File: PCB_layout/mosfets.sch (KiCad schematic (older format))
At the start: 45 parts, among them CN10 OUT, CN11 OUT, CN12 OUT, CN13 OUT, CN9 OUT, Q3 IRLR7843TRPBF, Q4 IRLR7843TRPBF, Q5 IRLR7843TRPBF, Q6 IRLR7843TRPBF, Q7 IRLR7843TRPBF

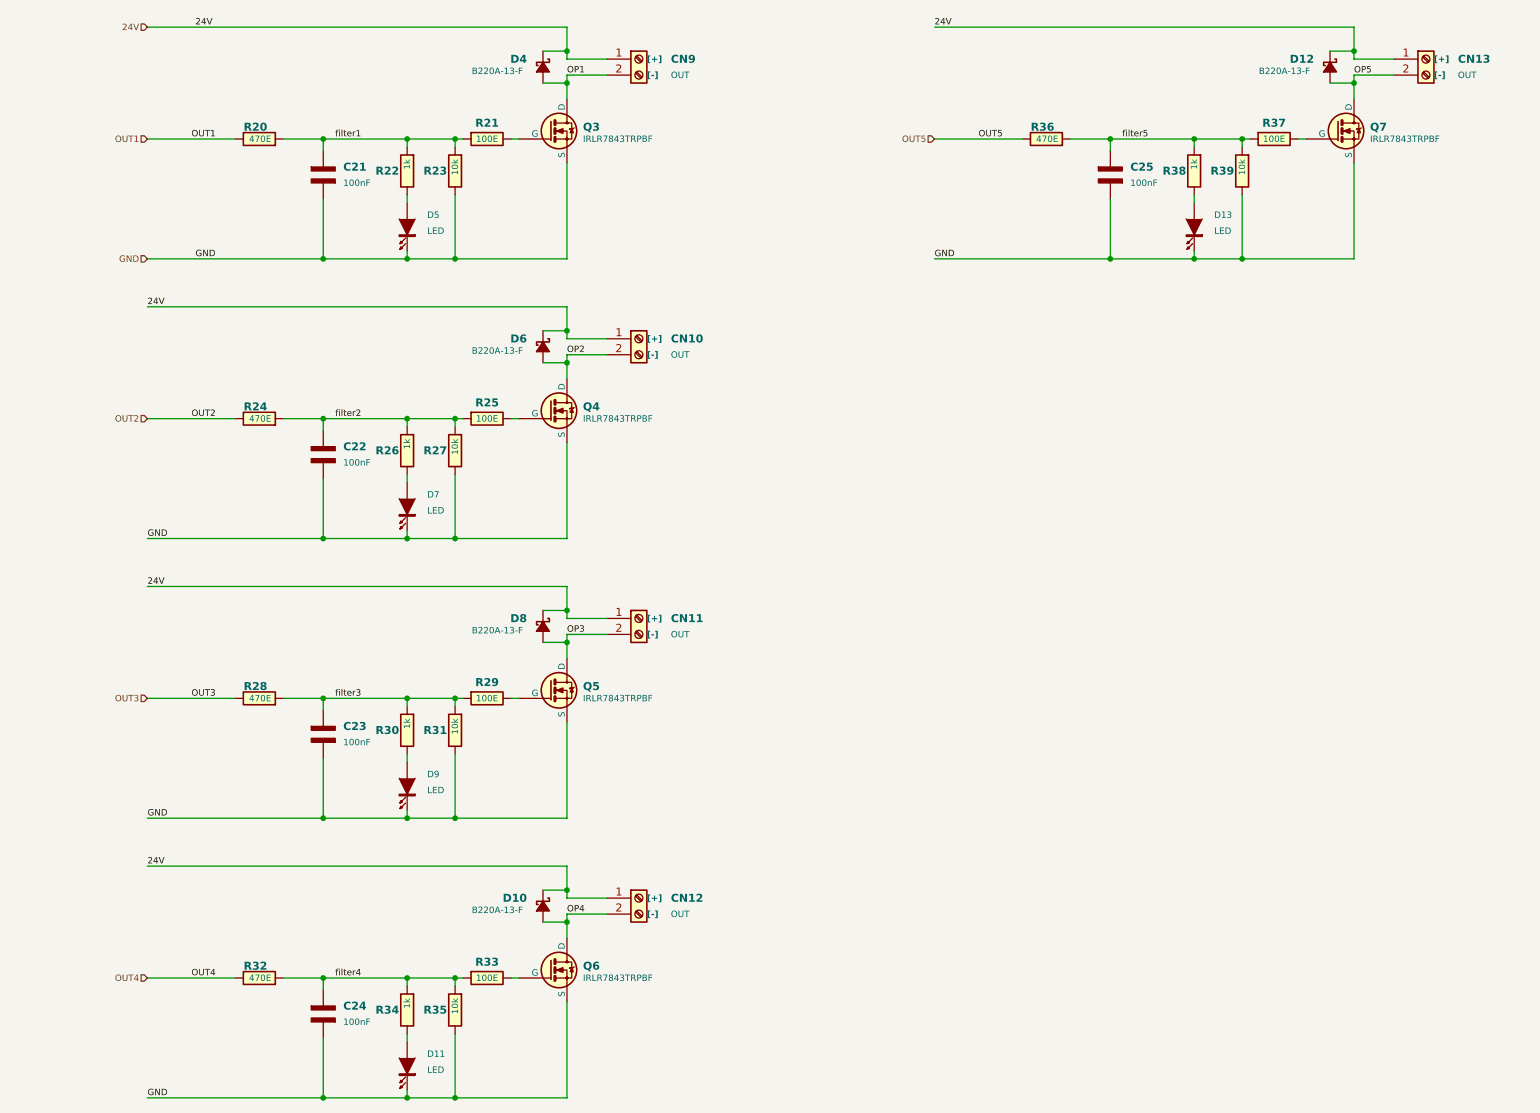
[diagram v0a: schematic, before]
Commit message: added optocoupler for isolation
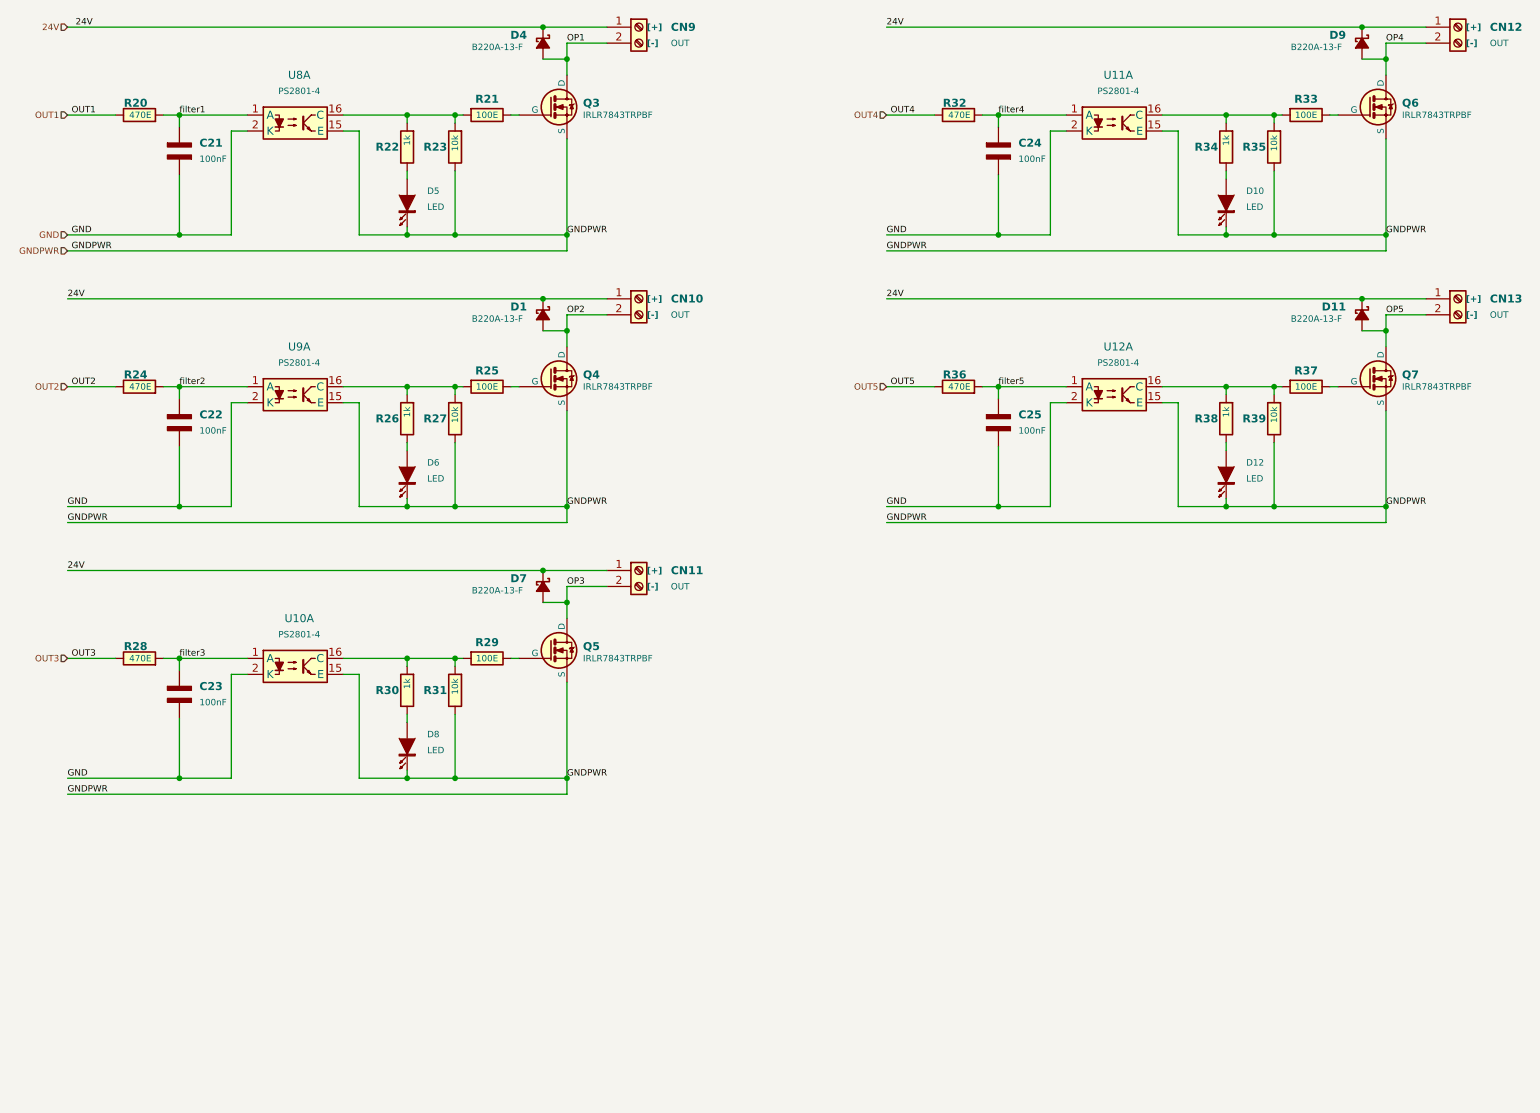
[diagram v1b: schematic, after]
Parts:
- removed D10, D12, D6, D8: B220A-13-F, AA_vayu:D_SMB, symbol AA_vayuO2_symbols:D_Schottky_Small
- removed D11, D13, D7, D9: LED, AA_vayu:LED_0603_1608Metric, symbol AA_vayuO2_symbols:LED
- added D1, D11, D7, D9: B220A-13-F, AA_vayu:D_SMB, symbol AA_vayuO2_symbols:D_Schottky_Small
- added D10, D12, D6, D8: LED, AA_vayu:LED_0603_1608Metric, symbol AA_vayuO2_symbols:LED
- added U10, U11, U12, U8, U9: PS2801-4, symbol AA_vayuO2_symbols:PS2801-4
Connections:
- net 24V: now also D1.1 (K), D11.1 (K), D7.1 (K), D9.1 (K)
- net GND: now also U10.2 (K), U11.2 (K), U12.2 (K), U8.2 (K), U9.2 (K); no longer D5.2 (K), Q3.3 (S), Q4.3 (S), Q5.3 (S), Q6.3 (S), Q7.3 (S), R23.1, R27.1, R31.1, R35.1, R39.1
- net OP2: now also D1.2 (A)
- net OP3: now also D7.2 (A)
- net OP4: now also D9.2 (A)
- net OP5: now also D11.2 (A)
- net filter1: now also U8.1 (A); no longer R21.2, R22.2, R23.2
- net filter2: now also U9.1 (A); no longer R25.2, R26.2, R27.2
- net filter3: now also U10.1 (A); no longer R29.2, R30.2, R31.2
- net filter4: now also U11.1 (A); no longer R33.2, R34.2, R35.2
- net filter5: now also U12.1 (A); no longer R37.2, R38.2, R39.2
- net at R26.1: now also D6.1 (A)
- net at R30.1: now also D8.1 (A)
- net at R34.1: now also D10.1 (A)
- net at R38.1: now also D12.1 (A)
- new net: R21.2, R22.2, R23.2, U8.16 (C)
- new net: R25.2, R26.2, R27.2, U9.16 (C)
- new net: R29.2, R30.2, R31.2, U10.16 (C)
- new net: R33.2, R34.2, R35.2, U11.16 (C)
- new net: R37.2, R38.2, R39.2, U12.16 (C)
- new net GNDPWR: D10.2 (K), D12.2 (K), D5.2 (K), D6.2 (K), D8.2 (K), Q3.3 (S), Q4.3 (S), Q5.3 (S), Q6.3 (S), Q7.3 (S), R23.1, R27.1, R31.1, R35.1, R39.1, U10.15 (E), U11.15 (E), U12.15 (E), U8.15 (E), U9.15 (E)
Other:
- moved on the sheet: C21, CN9, D4, D5, Q3, R20, R21, R22, R23

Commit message: PCB layout, WIP
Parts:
- U8: footprint (none) -> AA_vayu:SO-16_5.3x10.2mm_P1.27mm
- U8: renamed from U9; footprint (none) -> AA_vayu:SO-16_5.3x10.2mm_P1.27mm
- U8: renamed from U10; footprint (none) -> AA_vayu:SO-16_5.3x10.2mm_P1.27mm
- U8: renamed from U11; footprint (none) -> AA_vayu:SO-16_5.3x10.2mm_P1.27mm
- U9: renamed from U12; footprint (none) -> AA_vayu:SO-4_5.3x2.7mm_P1.27mm
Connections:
- net GND: now also U8.4 (K), U8.6 (K), U8.8 (K); no longer U8.2 (K), U8.2 (K), U8.2 (K)
- net GNDPWR: now also U8.11 (K), U8.13 (E), U8.9 (E); no longer U8.15 (E), U8.15 (E), U8.15 (E)
- net filter2: now also U8.3 (A); no longer U8.1 (A)
- net filter3: now also U8.5 (A); no longer U8.1 (A)
- net filter4: now also U8.7 (A); no longer U8.1 (A)
- net at R25.2, R26.2, R27.2: now also U8.14 (C); no longer U8.16 (C)
- net at R29.2, R30.2, R31.2: now also U8.12 (C); no longer U8.16 (C)
- net at R33.2, R34.2, R35.2: now also U8.10 (C); no longer U8.16 (C)
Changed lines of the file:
@@
 F 0 "U8" H 2350 1725 50  0000 C CNN
 F 1 "PS2801-4" H 2350 1625 40  0000 C CNN
-F 2 "" H 2325 1125 50  0001 C CIN
+F 2 "AA_vayu:SO-16_5.3x10.2mm_P1.27mm" H 2325 1125 50  0001 C CIN
 F 3 "" H 2300 1400 50  0001 L CNN
 	1    2325 1425
@@
 	4025 2725 4025 2625
 $Comp
-L AA_vayuO2_symbols:PS2801-4 U9
-U 1 1 61650FE4
+L AA_vayuO2_symbols:PS2801-4 U8
+U 2 1 61650FE4
 P 2325 3125
-F 0 "U9" H 2350 3425 50  0000 C CNN
+F 0 "U8" H 2350 3425 50  0000 C CNN
 F 1 "PS2801-4" H 2350 3325 40  0000 C CNN
-F 2 "" H 2325 2825 50  0001 C CIN
+F 2 "AA_vayu:SO-16_5.3x10.2mm_P1.27mm" H 2325 2825 50  0001 C CIN
 F 3 "" H 2300 3100 50  0001 L CNN
-	1    2325 3125
+	2    2325 3125
 	1    0    0    -1
 $EndComp
@@
 	4025 4425 4025 4325
 $Comp
-L AA_vayuO2_symbols:PS2801-4 U10
-U 1 1 6165FC0E
+L AA_vayuO2_symbols:PS2801-4 U8
+U 3 1 6165FC0E
 P 2325 4825
-F 0 "U10" H 2350 5125 50  0000 C CNN
+F 0 "U8" H 2350 5125 50  0000 C CNN
 F 1 "PS2801-4" H 2350 5025 40  0000 C CNN
-F 2 "" H 2325 4525 50  0001 C CIN
+F 2 "AA_vayu:SO-16_5.3x10.2mm_P1.27mm" H 2325 4525 50  0001 C CIN
 F 3 "" H 2300 4800 50  0001 L CNN
-	1    2325 4825
+	3    2325 4825
 	1    0    0    -1
 $EndComp
@@
 	9150 1025 9150 925
 $Comp
-L AA_vayuO2_symbols:PS2801-4 U11
-U 1 1 6165FCB0
+L AA_vayuO2_symbols:PS2801-4 U8
+U 4 1 6165FCB0
 P 7450 1425
-F 0 "U11" H 7475 1725 50  0000 C CNN
+F 0 "U8" H 7475 1725 50  0000 C CNN
 F 1 "PS2801-4" H 7475 1625 40  0000 C CNN
-F 2 "" H 7450 1125 50  0001 C CIN
+F 2 "AA_vayu:SO-16_5.3x10.2mm_P1.27mm" H 7450 1125 50  0001 C CIN
 F 3 "" H 7425 1400 50  0001 L CNN
-	1    7450 1425
+	4    7450 1425
 	1    0    0    -1
 $EndComp
@@
 	9150 2725 9150 2625
 $Comp
-L AA_vayuO2_symbols:PS2801-4 U12
+L AA_vayuO2_symbols:PS2801-4 U9
 U 1 1 6167D5CE
 P 7450 3125
-F 0 "U12" H 7475 3425 50  0000 C CNN
+F 0 "U9" H 7475 3425 50  0000 C CNN
 F 1 "PS2801-4" H 7475 3325 40  0000 C CNN
-F 2 "" H 7450 2825 50  0001 C CIN
+F 2 "AA_vayu:SO-4_5.3x2.7mm_P1.27mm" H 7450 2825 50  0001 C CIN
 F 3 "" H 7425 3100 50  0001 L CNN
 	1    7450 3125

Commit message: BOM, WIP
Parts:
- U9: value PS2801-4 -> PS2801-1
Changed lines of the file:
@@
 P 7450 3125
 F 0 "U9" H 7475 3425 50  0000 C CNN
-F 1 "PS2801-4" H 7475 3325 40  0000 C CNN
+F 1 "PS2801-1" H 7475 3325 40  0000 C CNN
 F 2 "AA_vayu:SO-4_5.3x2.7mm_P1.27mm" H 7450 2825 50  0001 C CIN
 F 3 "" H 7425 3100 50  0001 L CNN

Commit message: final production files generated
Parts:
- U10: renamed from U9; symbol AA_vayuO2_symbols:PS2801-4 -> AA_vayuO2_symbols:PS2801-1
- U12, U7, U9: renamed from U8; value PS2801-4 -> PS2801-1; footprint AA_vayu:SO-16_5.3x10.2mm_P1.27mm -> AA_vayu:SO-4_5.3x2.7mm_P1.27mm; symbol AA_vayuO2_symbols:PS2801-4 -> AA_vayuO2_symbols:PS2801-1
- U8: value PS2801-4 -> PS2801-1; footprint AA_vayu:SO-16_5.3x10.2mm_P1.27mm -> AA_vayu:SO-4_5.3x2.7mm_P1.27mm; symbol AA_vayuO2_symbols:PS2801-4 -> AA_vayuO2_symbols:PS2801-1
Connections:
- net GND: now also U12.2 (K), U8.2 (K), U9.2 (K); no longer U12.6 (K), U8.8 (K), U9.4 (K)
- net GNDPWR: now also U10.3 (E), U12.3 (E), U7.3 (E), U8.3 (E), U9.3 (E); no longer U10.15 (E), U12.11 (K), U7.15 (E), U8.9 (E), U9.13 (E)
- net filter2: now also U9.1 (A); no longer U9.3 (A)
- net filter3: now also U12.1 (A); no longer U12.5 (A)
- net filter4: now also U8.1 (A); no longer U8.7 (A)
- net at R21.2, R22.2, R23.2: now also U7.4 (C); no longer U7.16 (C)
- net at R25.2, R26.2, R27.2: now also U9.4 (C); no longer U9.14 (C)
- net at R29.2, R30.2, R31.2: now also U12.4 (C); no longer U12.12 (C)
- net at R33.2, R34.2, R35.2: now also U8.4 (C); no longer U8.10 (C)
- net at R37.2, R38.2, R39.2: now also U10.4 (C); no longer U10.16 (C)
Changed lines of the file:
@@
 	4025 1025 4025 925
 $Comp
-L AA_vayuO2_symbols:PS2801-4 U8
+L AA_vayuO2_symbols:PS2801-1 U7
 U 1 1 616348AD
 P 2325 1425
-F 0 "U8" H 2350 1725 50  0000 C CNN
-F 1 "PS2801-4" H 2350 1625 40  0000 C CNN
-F 2 "AA_vayu:SO-16_5.3x10.2mm_P1.27mm" H 2325 1125 50  0001 C CIN
+F 0 "U7" H 2350 1725 50  0000 C CNN
+F 1 "PS2801-1" H 2350 1625 40  0000 C CNN
+F 2 "AA_vayu:SO-4_5.3x2.7mm_P1.27mm" H 2325 1125 50  0001 C CIN
 F 3 "" H 2300 1400 50  0001 L CNN
 	1    2325 1425
@@
 	4025 2725 4025 2625
 $Comp
-L AA_vayuO2_symbols:PS2801-4 U8
-U 2 1 61650FE4
+L AA_vayuO2_symbols:PS2801-1 U9
+U 1 1 61650FE4
 P 2325 3125
-F 0 "U8" H 2350 3425 50  0000 C CNN
-F 1 "PS2801-4" H 2350 3325 40  0000 C CNN
-F 2 "AA_vayu:SO-16_5.3x10.2mm_P1.27mm" H 2325 2825 50  0001 C CIN
+F 0 "U9" H 2350 3425 50  0000 C CNN
+F 1 "PS2801-1" H 2350 3325 40  0000 C CNN
+F 2 "AA_vayu:SO-4_5.3x2.7mm_P1.27mm" H 2325 2825 50  0001 C CIN
 F 3 "" H 2300 3100 50  0001 L CNN
-	2    2325 3125
+	1    2325 3125
 	1    0    0    -1
 $EndComp
@@
 	4025 4425 4025 4325
 $Comp
-L AA_vayuO2_symbols:PS2801-4 U8
-U 3 1 6165FC0E
+L AA_vayuO2_symbols:PS2801-1 U12
+U 1 1 6165FC0E
 P 2325 4825
-F 0 "U8" H 2350 5125 50  0000 C CNN
-F 1 "PS2801-4" H 2350 5025 40  0000 C CNN
-F 2 "AA_vayu:SO-16_5.3x10.2mm_P1.27mm" H 2325 4525 50  0001 C CIN
+F 0 "U12" H 2350 5125 50  0000 C CNN
+F 1 "PS2801-1" H 2350 5025 40  0000 C CNN
+F 2 "AA_vayu:SO-4_5.3x2.7mm_P1.27mm" H 2325 4525 50  0001 C CIN
 F 3 "" H 2300 4800 50  0001 L CNN
-	3    2325 4825
+	1    2325 4825
 	1    0    0    -1
 $EndComp
@@
 	9150 1025 9150 925
 $Comp
-L AA_vayuO2_symbols:PS2801-4 U8
-U 4 1 6165FCB0
+L AA_vayuO2_symbols:PS2801-1 U8
+U 1 1 6165FCB0
 P 7450 1425
 F 0 "U8" H 7475 1725 50  0000 C CNN
-F 1 "PS2801-4" H 7475 1625 40  0000 C CNN
-F 2 "AA_vayu:SO-16_5.3x10.2mm_P1.27mm" H 7450 1125 50  0001 C CIN
+F 1 "PS2801-1" H 7475 1625 40  0000 C CNN
+F 2 "AA_vayu:SO-4_5.3x2.7mm_P1.27mm" H 7450 1125 50  0001 C CIN
 F 3 "" H 7425 1400 50  0001 L CNN
-	4    7450 1425
+	1    7450 1425
 	1    0    0    -1
 $EndComp
@@
 	9150 2725 9150 2625
 $Comp
-L AA_vayuO2_symbols:PS2801-4 U9
+L AA_vayuO2_symbols:PS2801-1 U10
 U 1 1 6167D5CE
 P 7450 3125
-F 0 "U9" H 7475 3425 50  0000 C CNN
+F 0 "U10" H 7475 3425 50  0000 C CNN
 F 1 "PS2801-1" H 7475 3325 40  0000 C CNN
 F 2 "AA_vayu:SO-4_5.3x2.7mm_P1.27mm" H 7450 2825 50  0001 C CIN
